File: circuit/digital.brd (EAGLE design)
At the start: 56.2 x 50.8 mm, 30 parts, among them IC1 MCP1701-5V, IC2 MCP1700-3.3V, X1 MINI-USB-SCHIELD-32005-301

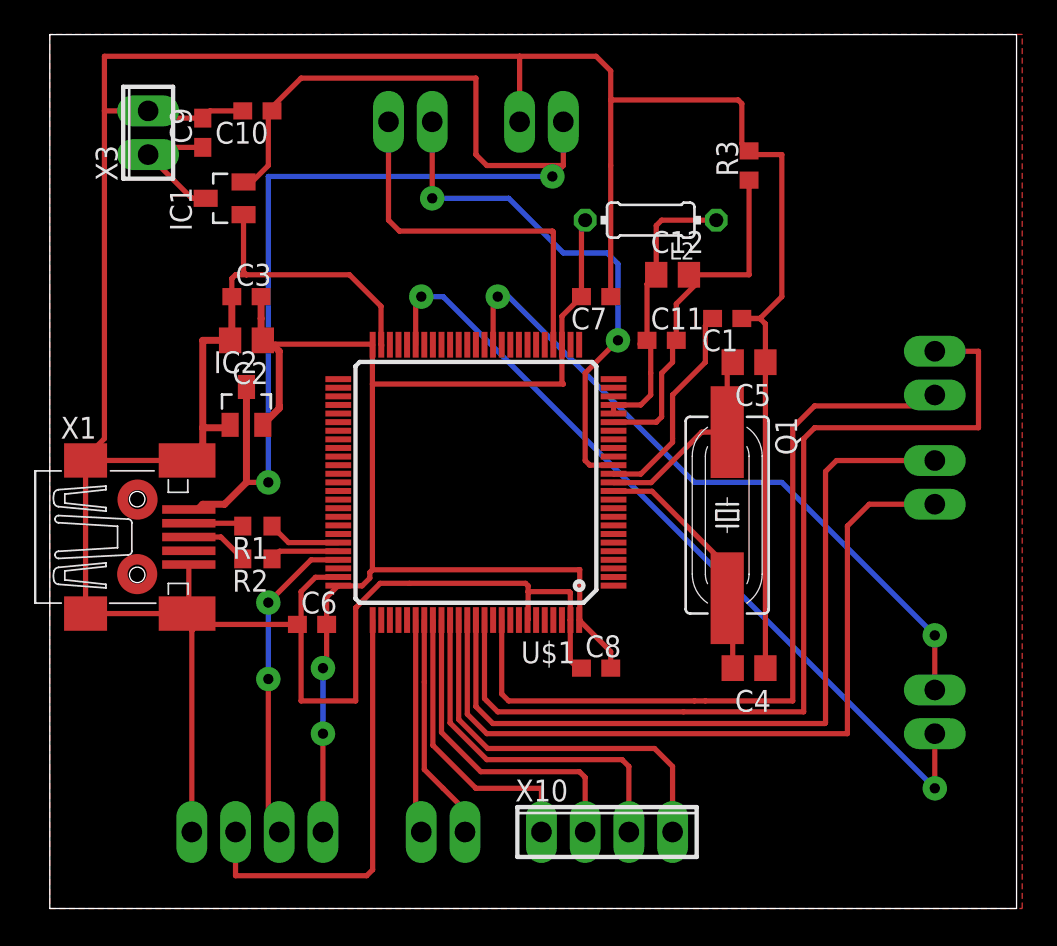
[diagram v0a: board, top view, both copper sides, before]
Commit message: - 0.25 мм выводы у STM32
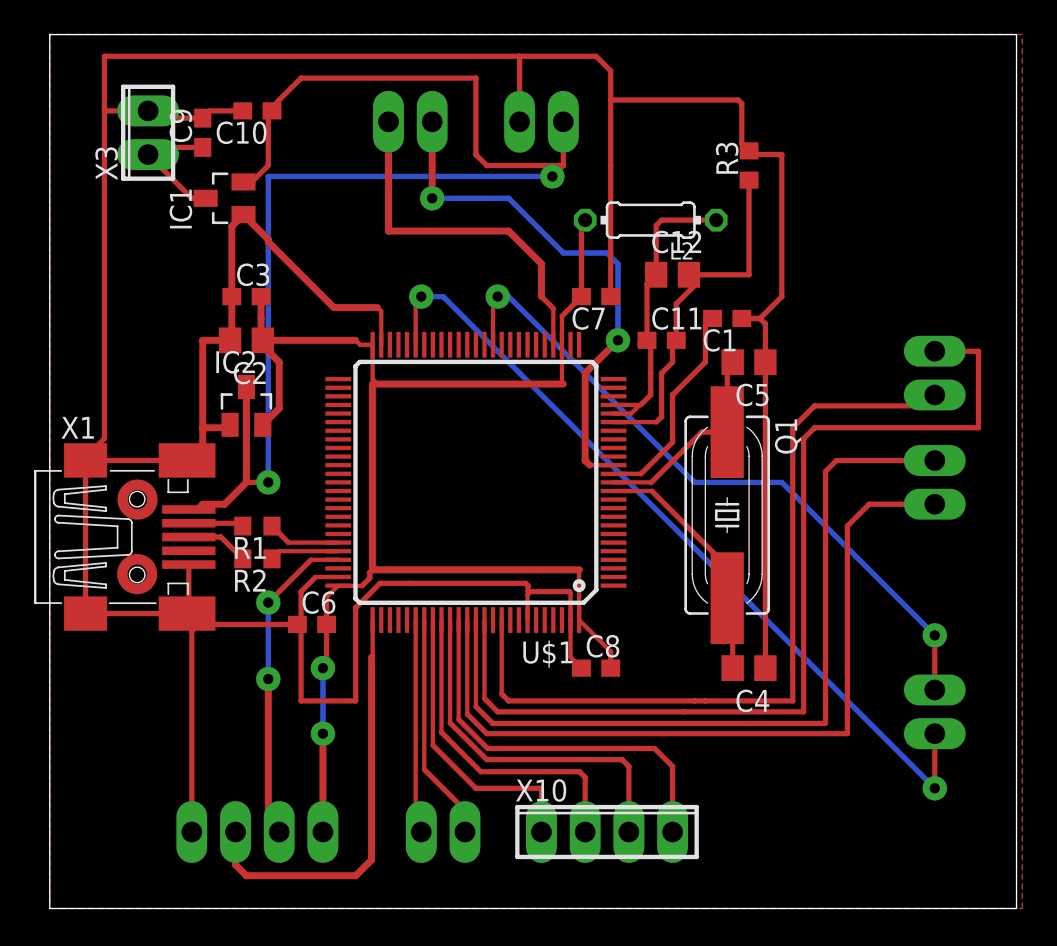
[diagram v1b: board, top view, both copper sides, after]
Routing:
- net V+: track 17.1 -> 18.4 mm
- net GENERATOR: track 22.1 -> 21.0 mm
- net GND: track 234.0 -> 234.9 mm
- net SWCLK: track 25.2 -> 24.4 mm
- net +3V3: track 84.4 -> 85.0 mm
- added copper zone on layer 1, net GND
- removed copper zone on layer 1, net GNDA

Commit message: - подтяжка по USB
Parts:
- added R4: 1.5k, rcl:R0603
- L2: value MMZ1608B102C -> 100mk
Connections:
- net +3V3: now also R4.1
- net GND: now also U$1.6
- net N$2: now also R4.2
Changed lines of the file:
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@@
 <layers>
 <layer number="1" name="Top" color="4" fill="1" visible="yes" active="yes"/>
-<layer number="16" name="Bottom" color="1" fill="1" visible="no" active="yes"/>
+<layer number="16" name="Bottom" color="1" fill="1" visible="yes" active="yes"/>
 <layer number="17" name="Pads" color="2" fill="1" visible="yes" active="yes"/>
 <layer number="18" name="Vias" color="2" fill="1" visible="yes" active="yes"/>
 <layer number="19" name="Unrouted" color="6" fill="1" visible="yes" active="yes"/>
-<layer number="20" name="Dimension" color="15" fill="1" visible="no" active="yes"/>
-<layer number="21" name="tPlace" color="7" fill="1" visible="no" active="yes"/>
-<layer number="22" name="bPlace" color="7" fill="1" visible="no" active="yes"/>
-<layer number="23" name="tOrigins" color="15" fill="1" visible="no" active="yes"/>
-<layer number="24" name="bOrigins" color="15" fill="1" visible="no" active="yes"/>
+<layer number="20" name="Dimension" color="15" fill="1" visible="yes" active="yes"/>
+<layer number="21" name="tPlace" color="7" fill="1" visible="yes" active="yes"/>
+<layer number="22" name="bPlace" color="7" fill="1" visible="yes" active="yes"/>
+<layer number="23" name="tOrigins" color="15" fill="1" visible="yes" active="yes"/>
+<layer number="24" name="bOrigins" color="15" fill="1" visible="yes" active="yes"/>
 <layer number="25" name="tNames" color="7" fill="1" visible="no" active="yes"/>
 <layer number="26" name="bNames" color="7" fill="1" visible="no" active="yes"/>
-<layer number="27" name="tValues" color="7" fill="1" visible="no" active="yes"/>
-<layer number="28" name="bValues" color="7" fill="1" visible="no" active="yes"/>
+<layer number="27" name="tValues" color="7" fill="1" visible="yes" active="yes"/>
+<layer number="28" name="bValues" color="7" fill="1" visible="yes" active="yes"/>
 <layer number="29" name="tStop" color="7" fill="3" visible="no" active="yes"/>
 <layer number="30" name="bStop" color="7" fill="6" visible="no" active="yes"/>
@@
 <layer number="35" name="tGlue" color="7" fill="4" visible="no" active="yes"/>
 <layer number="36" name="bGlue" color="7" fill="5" visible="no" active="yes"/>
-<layer number="37" name="tTest" color="7" fill="1" visible="no" active="yes"/>
-<layer number="38" name="bTest" color="7" fill="1" visible="no" active="yes"/>
-<layer number="39" name="tKeepout" color="4" fill="11" visible="no" active="yes"/>
-<layer number="40" name="bKeepout" color="1" fill="11" visible="no" active="yes"/>
-<layer number="41" name="tRestrict" color="4" fill="10" visible="no" active="yes"/>
-<layer number="42" name="bRestrict" color="1" fill="10" visible="no" active="yes"/>
-<layer number="43" name="vRestrict" color="2" fill="10" visible="no" active="yes"/>
-<layer number="44" name="Drills" color="7" fill="1" visible="no" active="yes"/>
-<layer number="45" name="Holes" color="7" fill="1" visible="no" active="yes"/>
-<layer number="46" name="Milling" color="3" fill="1" visible="no" active="yes"/>
-<layer number="47" name="Measures" color="7" fill="1" visible="no" active="yes"/>
-<layer number="48" name="Document" color="7" fill="1" visible="no" active="yes"/>
-<layer number="49" name="Reference" color="7" fill="1" visible="no" active="yes"/>
-<layer number="50" name="dxf" color="7" fill="1" visible="no" active="yes"/>
-<layer number="51" name="tDocu" color="7" fill="1" visible="no" active="yes"/>
-<layer number="52" name="bDocu" color="7" fill="1" visible="no" active="yes"/>
+<layer number="37" name="tTest" color="7" fill="1" visible="yes" active="yes"/>
+<layer number="38" name="bTest" color="7" fill="1" visible="yes" active="yes"/>
+<layer number="39" name="tKeepout" color="4" fill="11" visible="yes" active="yes"/>
+<layer number="40" name="bKeepout" color="1" fill="11" visible="yes" active="yes"/>
+<layer number="41" name="tRestrict" color="4" fill="10" visible="yes" active="yes"/>
+<layer number="42" name="bRestrict" color="1" fill="10" visible="yes" active="yes"/>
+<layer number="43" name="vRestrict" color="2" fill="10" visible="yes" active="yes"/>
+<layer number="44" name="Drills" color="7" fill="1" visible="yes" active="yes"/>
+<layer number="45" name="Holes" color="7" fill="1" visible="yes" active="yes"/>
+<layer number="46" name="Milling" color="3" fill="1" visible="yes" active="yes"/>
+<layer number="47" name="Measures" color="7" fill="1" visible="yes" active="yes"/>
+<layer number="48" name="Document" color="7" fill="1" visible="yes" active="yes"/>
+<layer number="49" name="Reference" color="7" fill="1" visible="yes" active="yes"/>
+<layer number="50" name="dxf" color="7" fill="1" visible="yes" active="yes"/>
+<layer number="51" name="tDocu" color="7" fill="1" visible="yes" active="yes"/>
+<layer number="52" name="bDocu" color="7" fill="1" visible="yes" active="yes"/>
 <layer number="91" name="Nets" color="2" fill="1" visible="no" active="no"/>
 <layer number="92" name="Busses" color="1" fill="1" visible="no" active="no"/>
@@
 <layer number="98" name="Guide" color="6" fill="1" visible="no" active="no"/>
 <layer number="100" name="Muster" color="7" fill="1" visible="no" active="no"/>
-<layer number="101" name="Patch_Top" color="12" fill="4" visible="no" active="yes"/>
-<layer number="116" name="Patch_BOT" color="9" fill="4" visible="no" active="yes"/>
+<layer number="101" name="Patch_Top" color="12" fill="4" visible="yes" active="yes"/>
+<layer number="116" name="Patch_BOT" color="9" fill="4" visible="yes" active="yes"/>
 <layer number="200" name="200bmp" color="1" fill="10" visible="no" active="no"/>
 <layer number="250" name="Descript" color="3" fill="1" visible="no" active="no"/>
 <layer number="251" name="SMDround" color="12" fill="11" visible="no" active="no"/>
-<layer number="254" name="cooling" color="7" fill="1" visible="no" active="yes"/>
+<layer number="254" name="cooling" color="7" fill="1" visible="yes" active="yes"/>
 </layers>
 <board>
@@
 </autorouter>
 <elements>
-<element name="L2" library="rcl" package="0204/7" value="MMZ1608B102C" x="34.925" y="40.005" rot="R180"/>
+<element name="L2" library="rcl" package="0204/7" value="100mk" x="34.925" y="40.005" rot="R180"/>
 <element name="C11" library="rcl" package="C0603" value="100n" x="35.56" y="33.02"/>
 <element name="C12" library="rcl" package="C0805" value="10mk" x="36.195" y="36.83"/>
@@
 <attribute name="OC_FARNELL" value="unknown" x="32.385" y="4.445" size="1.778" layer="27" display="off"/>
 </element>
+<element name="R4" library="rcl" package="R0603" value="1.5k" x="10.795" y="18.415" rot="R90"/>
 </elements>
 <signals>
@@
 <wire x1="8.08" y1="21.59" x2="9.945" y2="21.59" width="0.3048" layer="1"/>
 <wire x1="9.945" y1="21.59" x2="11.215" y2="20.32" width="0.3048" layer="1"/>
+<contactref element="R4" pad="2"/>
+<wire x1="10.795" y1="19.265" x2="11.215" y2="20.32" width="0" layer="19" extent="1-1"/>
 </signal>
 <signal name="USB_DM">
@@
 <wire x1="10.58" y1="35.56" x2="10.58" y2="39.645" width="0.4064" layer="1"/>
 <wire x1="10.58" y1="39.645" x2="11.26" y2="40.325" width="0.4064" layer="1"/>
+<contactref element="U$1" pad="6"/>
+<wire x1="30.265" y1="18.335" x2="32.765" y2="21.265" width="0" layer="19" extent="1-1"/>
+<wire x1="1.905" y1="26.035" x2="2.08" y2="26.04" width="0" layer="19" extent="1-1"/>
 </signal>
 <signal name="N$3">
@@
 <wire x1="29.765" y1="30.56" x2="29.845" y2="30.48" width="0.25" layer="1"/>
 <wire x1="29.765" y1="32.765" x2="29.765" y2="34.425" width="0.25" layer="1"/>
+<contactref element="R4" pad="1"/>
 <wire x1="16.78" y1="18.75" x2="16.765" y2="18.765" width="0" layer="19" extent="1-1"/>
+<wire x1="10.795" y1="17.565" x2="15.875" y2="4.445" width="0" layer="19" extent="1-1"/>
 </signal>
 <signal name="V+">

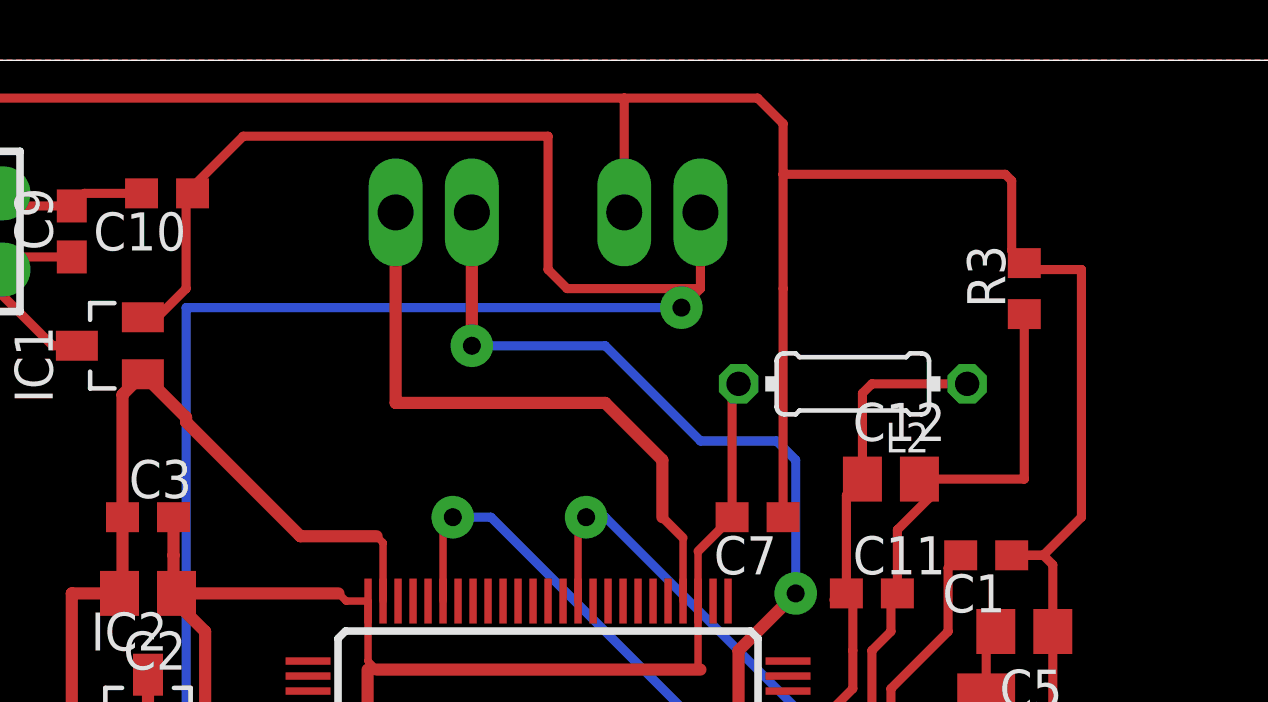
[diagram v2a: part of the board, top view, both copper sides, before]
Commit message: - стерли старые аналоговые схемы - стерли Hi Lo WaterMark
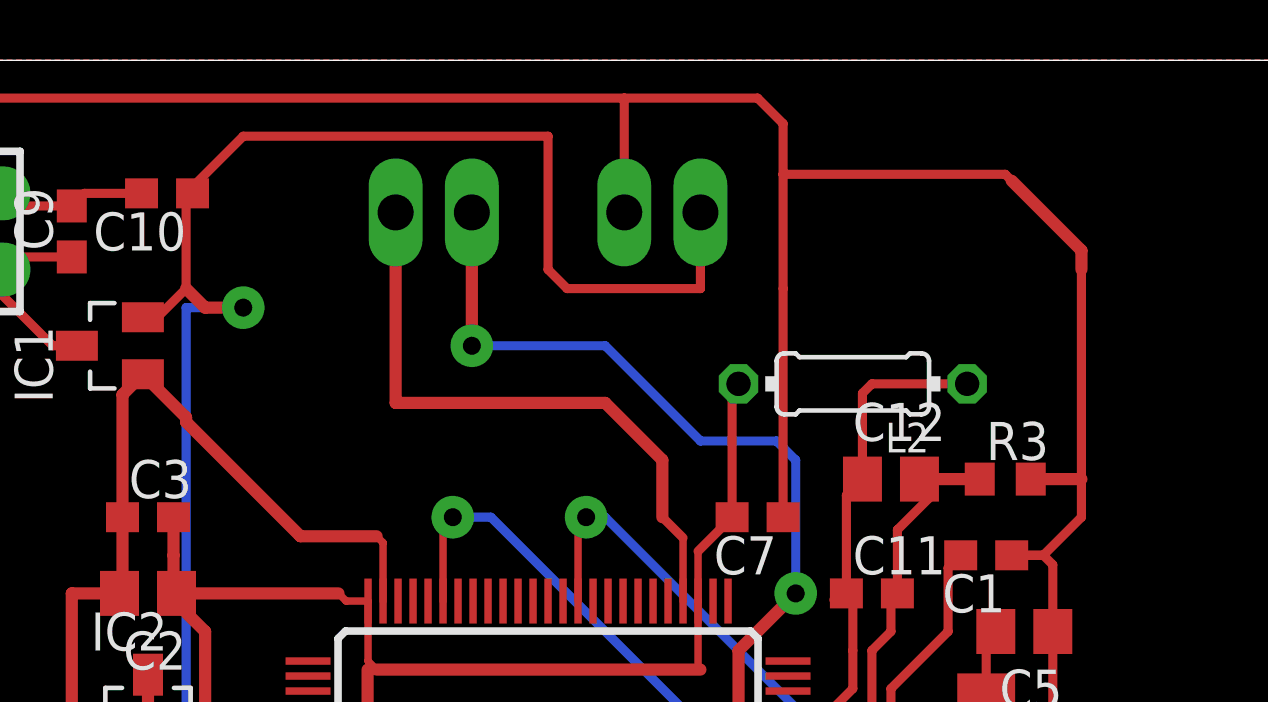
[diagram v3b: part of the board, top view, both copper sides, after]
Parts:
- moved R3 6.38 mm to (40.0, 36.8), turned to 0 degrees
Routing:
- net +5V: track 76.2 -> 62.9 mm
- net GNDA: track 21.5 -> 14.1 mm
- net GND: track 234.9 -> 235.6 mm
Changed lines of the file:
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@@
 <attribute name="OC_FARNELL" value="unknown" x="5.715" y="45.085" size="1.778" layer="27" rot="R90" display="off"/>
 </element>
-<element name="R3" library="rcl" package="R0603" value="0" x="40.64" y="43.18" rot="R90"/>
+<element name="R3" library="rcl" package="R0603" value="0" x="40.005" y="36.83"/>
 <element name="C9" library="rcl" package="C0603" value="1mk" x="8.89" y="45.085" rot="R90"/>
 <element name="C10" library="rcl" package="C0603" value="1mk" x="12.065" y="46.355" rot="R180"/>
@@
 <wire x1="8.585" y1="23.19" x2="8.08" y2="23.19" width="0.4064" layer="1"/>
 <wire x1="29.845" y1="45.72" x2="29.845" y2="43.18" width="0.3048" layer="1"/>
-<wire x1="29.845" y1="43.18" x2="29.21" y2="42.545" width="0.3048" layer="1"/>
-<via x="29.21" y="42.545" extent="1-16" drill="0.6" diameter="1.4224" shape="square"/>
+<via x="14.605" y="42.545" extent="1-16" drill="0.6" diameter="1.4224" shape="square"/>
 <via x="12.7" y="24.765" extent="1-16" drill="0.6" diameter="1.4224" shape="square"/>
 <wire x1="12.7" y1="24.765" x2="11.43" y2="24.765" width="0.3048" layer="1"/>
 <wire x1="12.7" y1="24.765" x2="12.7" y2="42.545" width="0.3048" layer="16"/>
-<wire x1="12.7" y1="42.545" x2="29.21" y2="42.545" width="0.3048" layer="16"/>
+<wire x1="12.7" y1="42.545" x2="14.605" y2="42.545" width="0.3048" layer="16"/>
 <contactref element="IC1" pad="2"/>
 <contactref element="C10" pad="1"/>
@@
 <wire x1="12.7" y1="43.18" x2="12.7" y2="46.14" width="0.3048" layer="1"/>
 <wire x1="12.7" y1="46.14" x2="12.915" y2="46.355" width="0.3048" layer="1"/>
+<wire x1="14.605" y1="42.545" x2="13.335" y2="42.545" width="0.4064" layer="1"/>
+<wire x1="13.335" y1="42.545" x2="12.7" y2="43.18" width="0.4064" layer="1"/>
 </signal>
 <signal name="GNDA">
@@
 <wire x1="37.465" y1="36.195" x2="37.465" y2="36.51" width="0.3048" layer="1"/>
 <wire x1="37.465" y1="36.51" x2="37.145" y2="36.83" width="0.3048" layer="1"/>
-<wire x1="40.64" y1="41.91" x2="40.64" y2="42.33" width="0.3048" layer="1"/>
-<wire x1="37.145" y1="36.83" x2="40.64" y2="36.83" width="0.3048" layer="1"/>
-<wire x1="40.64" y1="36.83" x2="40.64" y2="42.33" width="0.3048" layer="1"/>
 <wire x1="32.765" y1="28.265" x2="35.25" y2="28.265" width="0.25" layer="1"/>
+<wire x1="37.145" y1="36.83" x2="39.155" y2="36.83" width="0.4064" layer="1"/>
 </signal>
 <signal name="V_ADC">
@@
 <wire x1="6.135" y1="45.935" x2="5.715" y2="46.355" width="0.3048" layer="1"/>
 <wire x1="5.715" y1="46.355" x2="3.175" y2="46.355" width="0.3048" layer="1"/>
-<wire x1="40.22" y1="46.775" x2="40.22" y2="44.45" width="0.3048" layer="1"/>
-<wire x1="40.22" y1="44.45" x2="40.64" y2="44.03" width="0.3048" layer="1"/>
 <wire x1="40.22" y1="34.29" x2="41.275" y2="34.29" width="0.3048" layer="1"/>
 <wire x1="41.275" y1="34.29" x2="42.545" y2="35.56" width="0.3048" layer="1"/>
-<wire x1="42.545" y1="35.56" x2="42.545" y2="43.815" width="0.3048" layer="1"/>
-<wire x1="42.545" y1="43.815" x2="40.855" y2="43.815" width="0.3048" layer="1"/>
-<wire x1="40.855" y1="43.815" x2="40.64" y2="44.03" width="0.3048" layer="1"/>
+<wire x1="42.545" y1="35.56" x2="42.545" y2="36.83" width="0.3048" layer="1"/>
+<wire x1="42.545" y1="36.83" x2="42.545" y2="43.815" width="0.3048" layer="1"/>
 <contactref element="X9" pad="4"/>
 <wire x1="15.44" y1="19.25" x2="14.605" y2="18.415" width="0.3048" layer="1"/>
@@
 <wire x1="10.58" y1="39.645" x2="11.26" y2="40.325" width="0.4064" layer="1"/>
 <contactref element="U$1" pad="6"/>
-<wire x1="30.265" y1="18.335" x2="32.765" y2="21.265" width="0" layer="19" extent="1-1"/>
-<wire x1="1.905" y1="26.035" x2="2.08" y2="26.04" width="0" layer="19" extent="1-1"/>
+<wire x1="40.855" y1="36.83" x2="42.545" y2="36.83" width="0.4064" layer="1"/>
+<wire x1="2.08" y1="26.04" x2="1.905" y2="26.035" width="0" layer="19" extent="1-1"/>
+<wire x1="32.765" y1="21.265" x2="30.265" y2="18.335" width="0" layer="19" extent="1-1"/>
+<wire x1="42.545" y1="43.815" x2="42.545" y2="44.45" width="0.4064" layer="1"/>
+<wire x1="42.545" y1="44.45" x2="40.22" y2="46.775" width="0.4064" layer="1"/>
 </signal>
 <signal name="N$3">
